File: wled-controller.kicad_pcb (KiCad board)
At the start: 2 copper layers, 110 x 40 mm, 41 parts, among them J1 Screw_Terminal_01x04, J2 Screw_Terminal_01x06, J3 Conn_01x05_Male, SW1 SW_Push, SW2 SW_Push, U1 LM1117-3.3, U2 74HCT00, U3 ESP-07, U4 TSOP45xx, U5 TSOP17xx

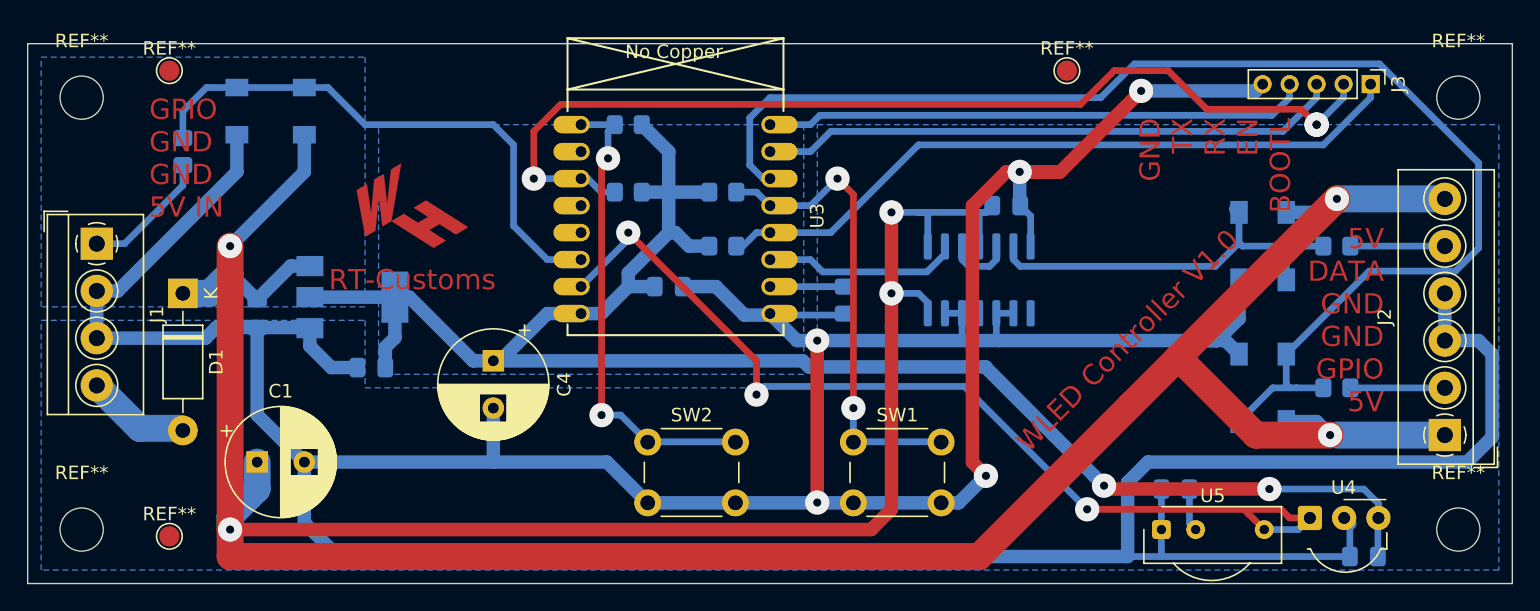
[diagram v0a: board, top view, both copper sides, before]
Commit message: Rev 2 with open Collector PS switch
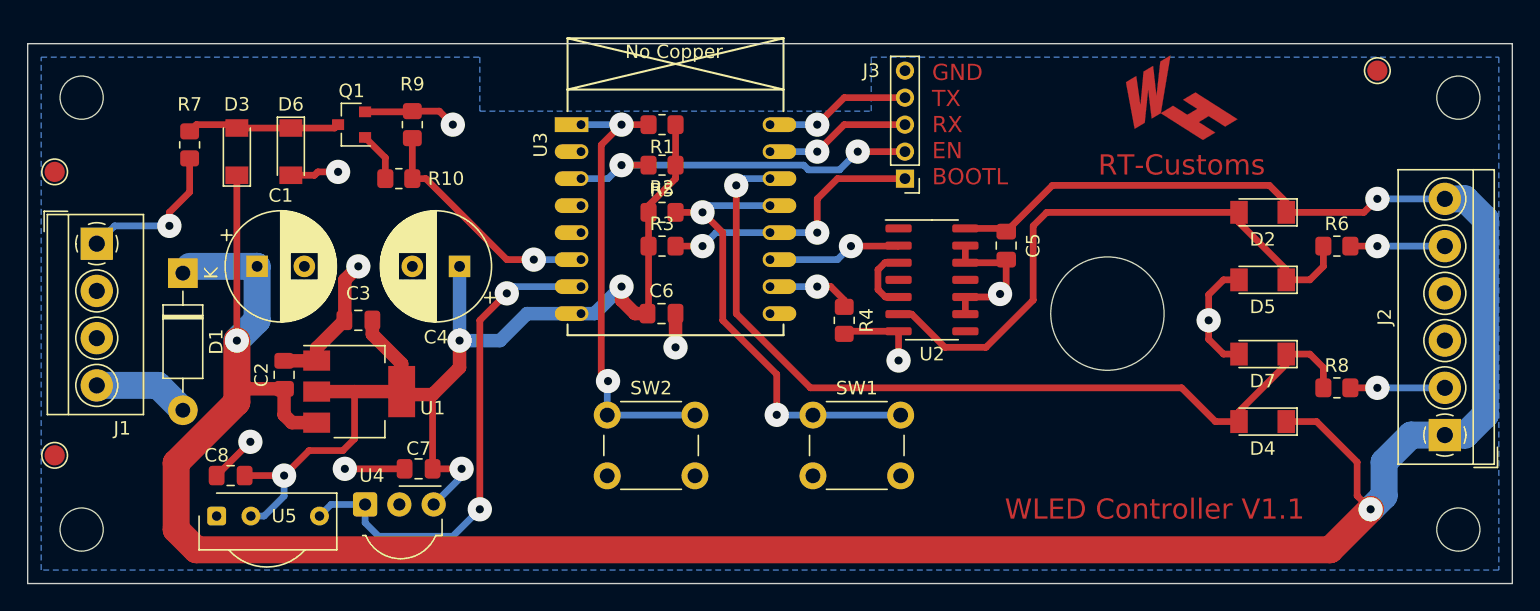
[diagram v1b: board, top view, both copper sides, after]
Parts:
- added Q1: BC817, Package_TO_SOT_SMD:SOT-23, F.Cu at (94.0, 76.0)
- added R10: 1k2, Resistor_SMD:R_0805_2012Metric_Pad1.20x1.40mm_HandSolder, F.Cu at (97.5, 80.0)
- added R9: 10k, Resistor_SMD:R_0805_2012Metric_Pad1.20x1.40mm_HandSolder, F.Cu at (98.5, 76.0)
- added REF**: MountingHole_8.4mm_M8, MountingHole:MountingHole_8.4mm_M8, B.Cu at (150.0, 90.0)
- C2, C3, C5, C6, C7, C8, D2, D3, D4, D5, D6, D7, R1, R2, R3, R4, R5, R6, R7, R8, U1, U2: moved to F.Cu
- U3: footprint ESP8266:ESP-07_tht -> ESP8266:ESP-07v2
- moved C7 70.3 mm to (99.0, 101.5)
- moved C8 70.0 mm to (85.0, 102.0)
- moved U4 70.0 mm to (95.0, 104.1)
- moved U5 70.0 mm to (84.0, 105.0)
- moved G*** 57.6 mm to (155.5, 74.0)
- moved J3 35.2 mm to (135.0, 80.0), turned to 180 degrees
- moved REF** 23.0 mm to (170.0, 72.0)
- moved C1 14.5 mm to (87.0, 86.5)
- moved REF** 11.3 mm to (72.0, 79.5)
- moved REF** 10.4 mm to (72.0, 100.5)
- moved C4 7.43 mm to (102.0, 86.5), turned to 180 degrees
- moved U1 7.02 mm to (94.6, 95.8)
- moved D3 5.83 mm to (85.5, 78.0)
- moved D6 5.00 mm to (89.5, 78.0)
- moved C2 4.96 mm to (89.0, 94.5), turned to 90 degrees
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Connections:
- net RELAY_OUT renamed PS_ON
- D3 pad 2: ESP_RELAY -> Net-(D3-Pad2)
- D6 pad 1: ESP_RELAY -> Net-(D3-Pad2)
- R7 pad 1: ESP_RELAY -> Net-(D3-Pad2)
- U3 pad 6: ESP_RELAY -> ESP_PS_ON
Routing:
- net GND: track 379.3 -> 57.8 mm, vias 5 -> 9
- net +3V3: track 140.9 -> 85.6 mm, vias 2 -> 4
- net +5V: track 273.6 -> 221.6 mm, vias 6 -> 3
- net ESP_EN: track 75.3 -> 27.1 mm, vias 3 -> 2
- net ESP_RELAY: track 41.0 -> 0.00 mm
- net ESP_IR: track 73.0 -> 37.4 mm, vias 3 -> 2
- net ESP_SW2: track 97.8 -> 63.9 mm, vias 0 -> 1
- net ESP_RX: track 43.2 -> 10.8 mm, vias 0 -> 1
- net ESP_BOOTL: track 52.6 -> 20.5 mm, vias 0 -> 2
- net ESP_TX: track 40.3 -> 10.8 mm, vias 0 -> 1
- net ESP_PS_ON: track 0.00 -> 18.0 mm, vias 0 -> 1
- net 5V_LED_DATA: track 30.2 -> 44.7 mm
- net Net-(D3-Pad2): track 0.00 -> 11.4 mm
- net ESP_LED_DATA: track 14.4 -> 9.96 mm, vias 0 -> 1
- net Net-(Q1-Pad1): track 0.00 -> 3.67 mm
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- removed copper zone on B.Cu, net +3V3
- removed copper zone on B.Cu, net +5V
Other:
- board text added: "WLED Controller V1.1"
- board text removed: "5V DATA GND GND GPIO 5V"
- board text removed: "GPIO GND GND 5V IN"
- board text removed: "WLED Controller V1.0"

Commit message: Moved ESP to not stick over board side.
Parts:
- moved C6 0.50 mm to (117.0, 90.5)
- moved R1 0.50 mm to (117.0, 76.5)
- moved R2 0.50 mm to (117.0, 79.5)
- moved R3 0.50 mm to (117.0, 85.5)
- moved R5 0.50 mm to (117.0, 83.0)
- moved U3 0.50 mm to (111.0, 76.5)
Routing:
- net ESP_SW1: track 33.7 -> 33.2 mm
- net ESP_BOOTL: track 20.5 -> 21.0 mm
